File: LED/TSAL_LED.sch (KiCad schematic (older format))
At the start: 69 parts, among them J1 Mini-SPOX, Q1 Q_PMOS_GSD, U2 XC9141

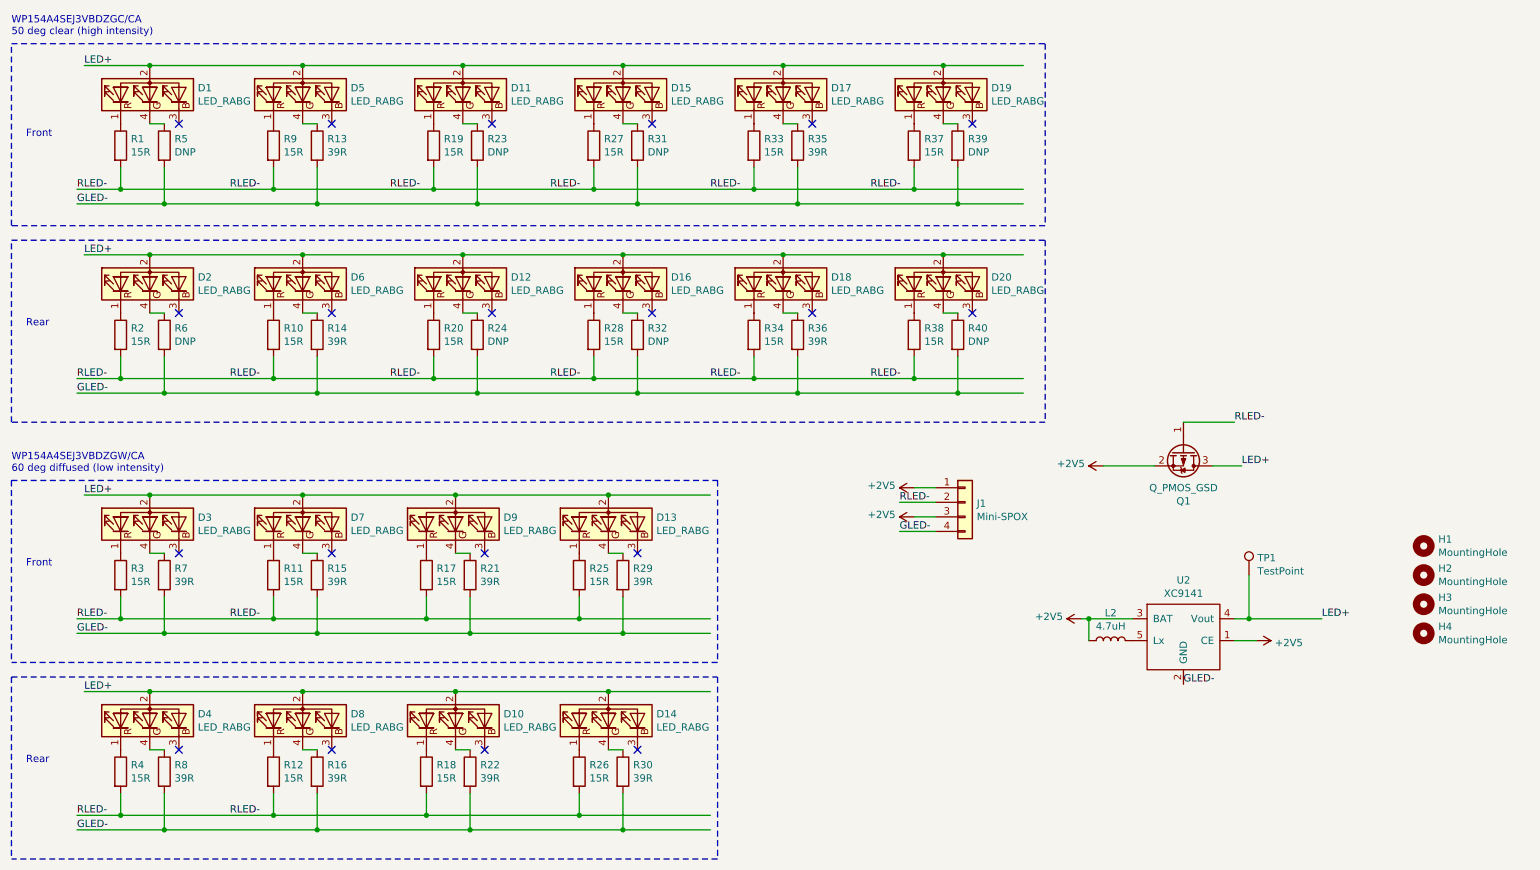
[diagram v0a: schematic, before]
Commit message: Move LED board files
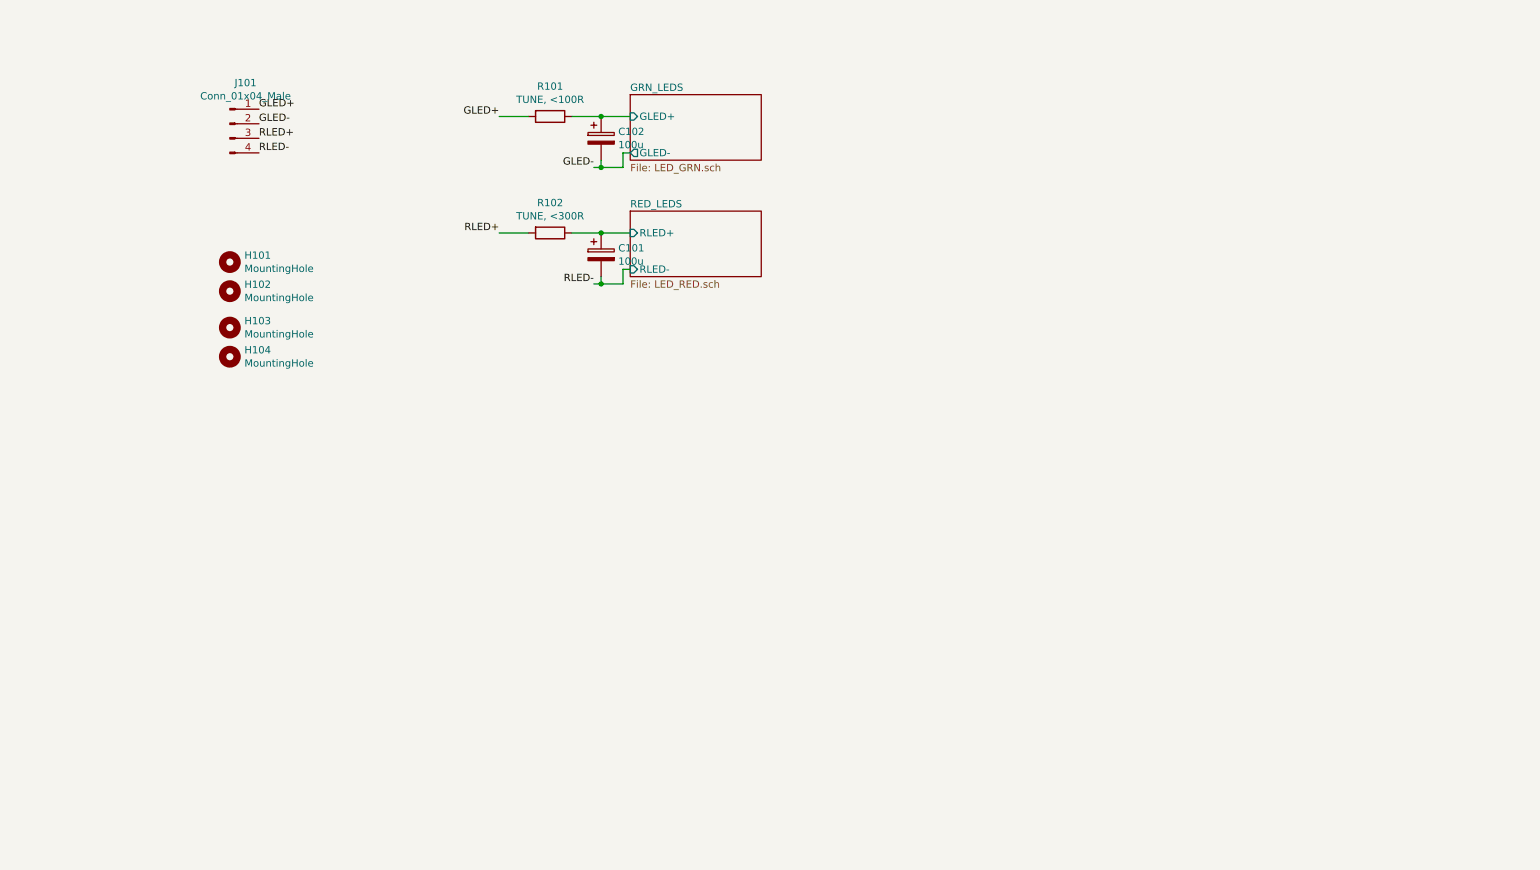
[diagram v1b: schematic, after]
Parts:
- removed D1, D10, D11, D12, D13, D14, D15, D16, D17, D18, D19, D2, D20, D3, D4, D5, D6, D7, D8, D9: LED_RABG, LED_THT:LED_D5.0mm-4_RGB, symbol Device:LED_RABG
- removed H1, H2, H3, H4: MountingHole, MountingHole:MountingHole_3.2mm_M3_Pad, symbol Mechanical:MountingHole
- removed J1: Mini-SPOX, Connector_Molex:Molex_SPOX_5267-04A_1x04_P2.50mm_Vertical, symbol Connector_Generic:Conn_01x04
- removed L2: 4.7uH, Inductor_SMD:L_Coilcraft_LPS5030, symbol Device:L
- removed Q1: Q_PMOS_GSD, Package_TO_SOT_SMD:SOT-23, symbol Device:Q_PMOS_GSD
- removed R1, R10, R11, R12, R17, R18, R19, R2, R20, R25, R26, R27, R28, R3, R33, R34, R37, R38, R4, R9: 15R, Resistor_SMD:R_0603_1608Metric_Pad1.05x0.95mm_HandSolder, symbol Device:R
- removed R13, R14, R15, R16, R21, R22, R29, R30, R35, R36, R7, R8: 39R, Resistor_SMD:R_0603_1608Metric_Pad1.05x0.95mm_HandSolder, symbol Device:R
- removed R23, R24, R31, R32, R39, R40, R5, R6: DNP, Resistor_SMD:R_0603_1608Metric_Pad1.05x0.95mm_HandSolder, symbol Device:R
- removed TP1: TestPoint, TestPoint:TestPoint_Pad_D3.0mm, symbol Connector:TestPoint
- removed U2: XC9141, Package_TO_SOT_SMD:SOT-23-5_HandSoldering, symbol xc9141:XC9141
- added C101, C102: 100u, Capacitor_SMD:CP_Elec_6.3x5.8, symbol Device:CP
- added H101, H102, H103, H104: MountingHole, MountingHole:MountingHole_3.2mm_M3_DIN965_Pad_TopBottom, symbol Mechanical:MountingHole
- added J101: Conn_01x04_Male, Connector_Molex:Molex_SPOX_5267-04A_1x04_P2.50mm_Vertical, symbol Connector:Conn_01x04_Male
- added R101: TUNE, <100R, Resistor_SMD:R_1206_3216Metric_Pad1.30x1.75mm_HandSolder, symbol Device:R
- added R102: TUNE, <300R, Resistor_SMD:R_1206_3216Metric_Pad1.30x1.75mm_HandSolder, symbol Device:R
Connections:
- net labels added: GLED+, RLED+
- net labels removed: +2V5, LED+
- wire segments 146 -> 16
- no-connect marks 20 -> 0
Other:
- note removed: "Front"
- note removed: "Rear"
- note removed: "WP154A4SEJ3VBDZGC/CA\n50 deg clear (high intensity)"
- note removed: "WP154A4SEJ3VBDZGW/CA\n60 deg diffused (low intensity)"
